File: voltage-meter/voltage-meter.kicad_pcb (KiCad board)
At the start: 4 copper layers, 46.2 x 96.2 mm, 56 parts, among them J1 Bannana plug, J2 Bannana plug, J3 I2C, J4 UART, J5 SPI, J6 PSU, J7 CTRL, J8 Conn_02x08_Odd_Even, Q1 MMBT2222A, Q2 MMBT2222A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

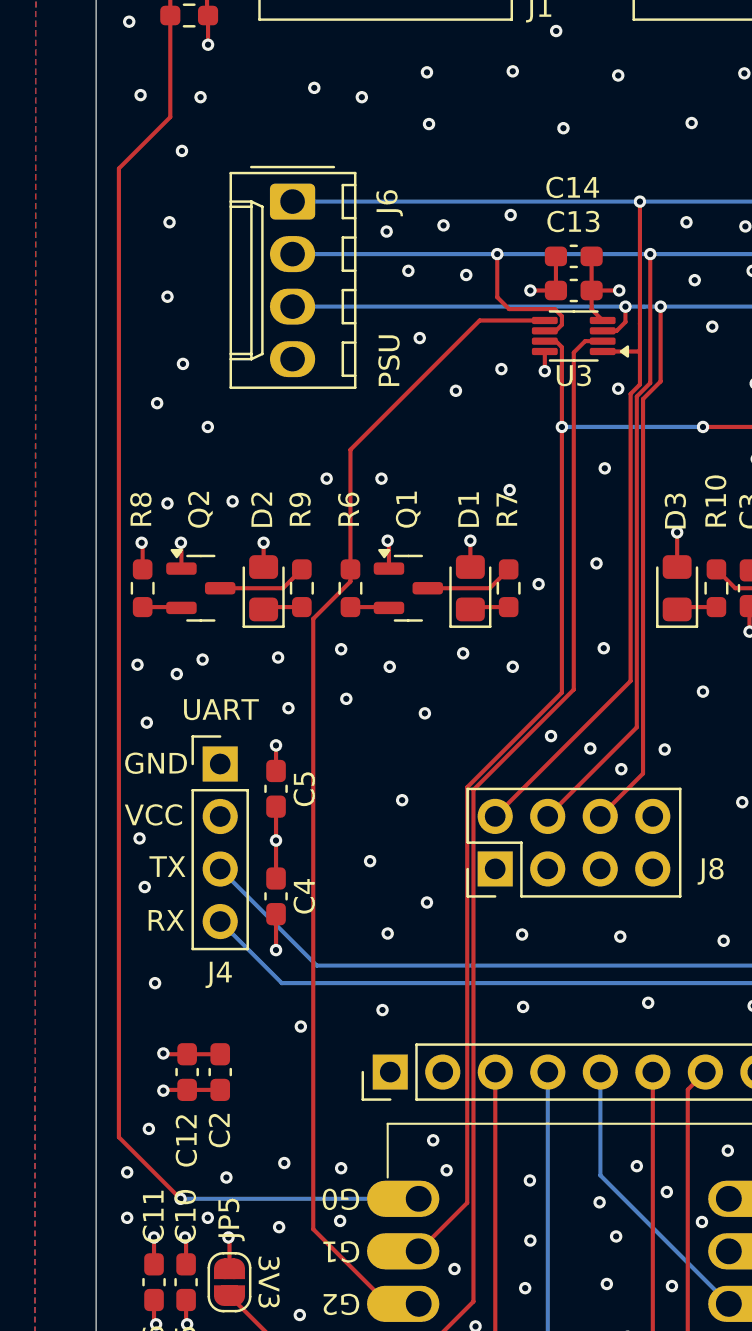
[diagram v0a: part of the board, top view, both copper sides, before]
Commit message: rusty-boards: voltage-meter: Update PCB for manufacturing
- bump board revision to v0.2
- update trace routing and via placement
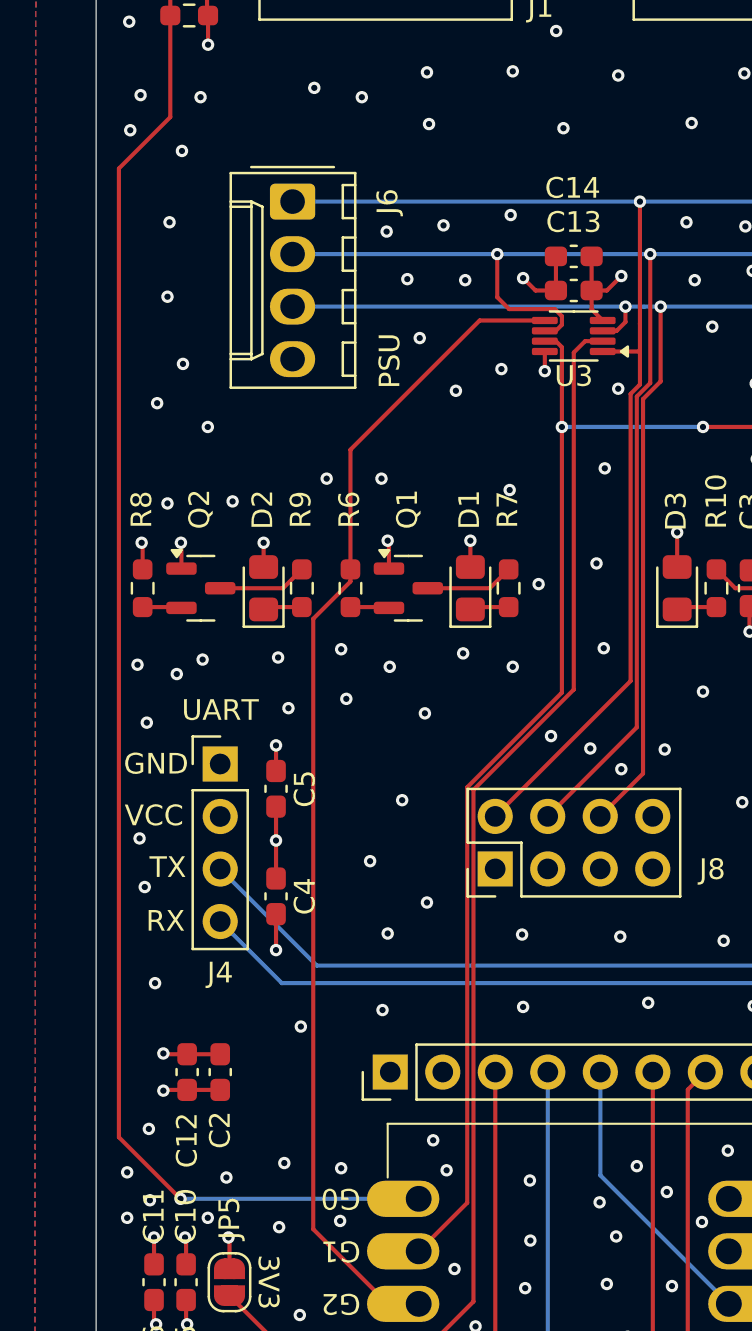
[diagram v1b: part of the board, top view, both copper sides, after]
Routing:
- net VCC: track 38.4 -> 39.0 mm
- net GND: track 38.2 -> 38.6 mm, vias 205 -> 207
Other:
- board text added: "PSU-SNIFFER v0.2 2505xx JKR"
- board text removed: "PSU-SNIFFER v0.1 250423 JKR"
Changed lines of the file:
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@@
 		(layer "Edge.Cuts")
 	)
-	(gr_text "PSU-SNIFFER\nv0.1 250423\nJKR"
+	(gr_text "PSU-SNIFFER\nv0.2 2505xx\nJKR"
 		(at 104.1 133.8 180)
 		(layer "B.SilkS")
@@
 	)
 	(segment
-		(start 104.9625 82.5)
-		(end 106.3 82.5)
-		(width 0.2)
-		(layer "F.Cu")
-		(net 2)
-	)
-	(segment
 		(start 85.35 132.35)
 		(end 85.35 131.325)
@@
 	)
 	(segment
+		(start 104.9625 82.5)
+		(end 105.7 82.5)
+		(width 0.2)
+		(layer "F.Cu")
+		(net 2)
+	)
+	(segment
 		(start 120.04 121.24)
 		(end 120 121.2)
@@
 	)
 	(segment
+		(start 105.7 82.5)
+		(end 106.4 81.8)
+		(width 0.2)
+		(layer "F.Cu")
+		(net 2)
+	)
+	(segment
 		(start 104.9625 82.5)
 		(end 104.9625 83.4125)
@@
 	)
 	(via
+		(at 83.6 126.5)
+		(size 0.6)
+		(drill 0.3)
+		(layers "F.Cu" "B.Cu")
+		(free yes)
+		(net 2)
+	)
+	(via
 		(at 124.3 100.45)
 		(size 0.6)
@@
 	)
 	(via
+		(at 82.65 74.75)
+		(size 0.6)
+		(drill 0.3)
+		(layers "F.Cu" "B.Cu")
+		(free yes)
+		(net 2)
+	)
+	(via
 		(at 106.25 87.25)
 		(size 0.6)
@@
 	)
 	(via
-		(at 96.1 81.55)
+		(at 96.05 81.95)
 		(size 0.6)
 		(drill 0.3)
@@
 	)
 	(via
-		(at 106.3 82.5)
+		(at 106.4 81.8)
 		(size 0.6)
 		(drill 0.3)
@@
 	)
 	(via
-		(at 98.9 81.75)
+		(at 98.85 82)
 		(size 0.6)
 		(drill 0.3)
@@
 	)
 	(segment
+		(start 103.2375 82.5)
+		(end 102.25 82.5)
+		(width 0.2)
+		(layer "F.Cu")
+		(net 16)
+	)
+	(segment
 		(start 83.8 129.6)
 		(end 83.8 128.3)
@@
 	)
 	(segment
-		(start 103.2375 82.5)
-		(end 102 82.5)
+		(start 102.25 82.5)
+		(end 101.65 81.9)
 		(width 0.2)
 		(layer "F.Cu")
@@
 	)
 	(via
-		(at 102 82.5)
+		(at 101.65 81.9)
 		(size 0.6)
 		(drill 0.3)
@@
 			(vias allowed)
 			(pads not_allowed)
-			(copperpour not_allowed)
+			(copperpour allowed)
 			(footprints not_allowed)
 		)
@@
 			(vias allowed)
 			(pads not_allowed)
-			(copperpour not_allowed)
+			(copperpour allowed)
 			(footprints not_allowed)
 		)
 		(placement
 			(enabled no)
-			(sheetname "")
+			(sheetname "/")
 		)
 		(fill
@@
 			(vias allowed)
 			(pads not_allowed)
-			(copperpour not_allowed)
+			(copperpour allowed)
 			(footprints not_allowed)
 		)
@@
 			(vias allowed)
 			(pads not_allowed)
-			(copperpour not_allowed)
+			(copperpour allowed)
 			(footprints not_allowed)
 		)
@@
 			(vias allowed)
 			(pads not_allowed)
-			(copperpour not_allowed)
+			(copperpour allowed)
 			(footprints not_allowed)
 		)
 		(placement
 			(enabled no)
-			(sheetname "")
+			(sheetname "/")
 		)
 		(fill
@@
 			(vias allowed)
 			(pads allowed)
-			(copperpour not_allowed)
+			(copperpour allowed)
 			(footprints not_allowed)
 		)
 		(placement
 			(enabled no)
-			(sheetname "")
+			(sheetname "/")
 		)
 		(fill
@@
 			(vias allowed)
 			(pads not_allowed)
-			(copperpour not_allowed)
+			(copperpour allowed)
 			(footprints not_allowed)
 		)
@@
 			(vias allowed)
 			(pads not_allowed)
-			(copperpour not_allowed)
+			(copperpour allowed)
 			(footprints not_allowed)
 		)
@@
 			(vias allowed)
 			(pads not_allowed)
-			(copperpour not_allowed)
+			(copperpour allowed)
 			(footprints not_allowed)
 		)
@@
 			(vias allowed)
 			(pads not_allowed)
-			(copperpour not_allowed)
+			(copperpour allowed)
 			(footprints not_allowed)
 		)
 		(placement
 			(enabled no)
-			(sheetname "")
+			(sheetname "/")
 		)
 		(fill
@@
 			(vias allowed)
 			(pads not_allowed)
-			(copperpour not_allowed)
+			(copperpour allowed)
 			(footprints not_allowed)
 		)
@@
 			(vias allowed)
 			(pads not_allowed)
-			(copperpour not_allowed)
+			(copperpour allowed)
 			(footprints not_allowed)
 		)
 		(placement
 			(enabled no)
-			(sheetname "")
+			(sheetname "/")
 		)
 		(fill
@@
 			(vias allowed)
 			(pads allowed)
-			(copperpour not_allowed)
+			(copperpour allowed)
 			(footprints not_allowed)
 		)
 		(placement
 			(enabled no)
-			(sheetname "")
+			(sheetname "/")
 		)
 		(fill
@@
 			(vias allowed)
 			(pads allowed)
-			(copperpour not_allowed)
+			(copperpour allowed)
 			(footprints not_allowed)
 		)
@@
 			(vias not_allowed)
 			(pads not_allowed)
-			(copperpour not_allowed)
+			(copperpour allowed)
 			(footprints not_allowed)
 		)
 		(placement
 			(enabled no)
-			(sheetname "")
+			(sheetname "/")
 		)
 		(fill
@@
 		(placement
 			(enabled no)
-			(sheetname "")
+			(sheetname "/")
 		)
 		(fill

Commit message: rusty-boards: voltage-meter: Reassign footprints to shared library
- reassign R1-R13 from Resistor_SMD to rusty-boards:R-0603-HandSolder
- reassign C1-C16 from Capacitor_SMD to rusty-boards:C-0603-HandSolder
- reassign Q1-Q5 from Package_TO_SOT_SMD to rusty-boards:SOT-23
- exclude remaining lib_footprint_mismatch for D1-D3 and J6-J7
- remove stale DRC exclusions for replaced footprints
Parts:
- C1, C10, C11, C12, C13, C14, C15, C16, C2, C3, C4, C5, C6, C7, C8, C9: footprint Capacitor_SMD:C_0603_1608Metric_Pad1.08x0.95mm_HandSolder -> rusty-boards:C-0603-HandSolder
- Q1, Q2, Q4, Q5: footprint Package_TO_SOT_SMD:SOT-23 -> rusty-boards:SOT-23
- R1, R10, R11, R12, R13, R2, R3, R4, R5, R6, R7, R8, R9: footprint Resistor_SMD:R_0603_1608Metric_Pad0.98x0.95mm_HandSolder -> rusty-boards:R-0603-HandSolder
